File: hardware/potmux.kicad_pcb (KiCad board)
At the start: 2 copper layers, 22.9 x 29.2 mm, 8 parts, among them P1 SOCKET_LEFT, P3 SOCKET_RIGHT, P4 KEYMAN64, U1 4052, U2 4052

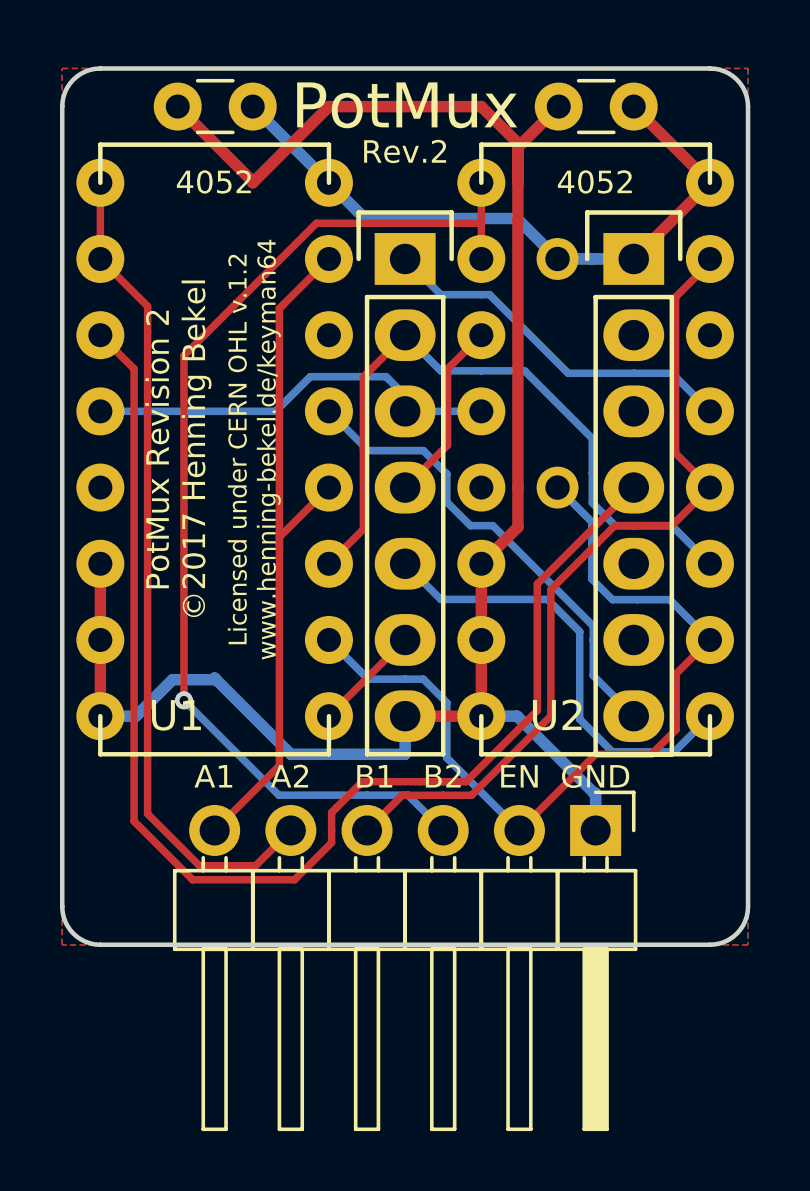
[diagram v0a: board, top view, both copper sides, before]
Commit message: Changes in preparation for release
- Changed Licenses to MIT-style licensing schemes
- Removed files required by cern ohl
- Rerendered schematic svg
- Improved silkscreen, updated last name and Copyright notices
- Adjustments for KiCAD 5.x
- Improved Makefile
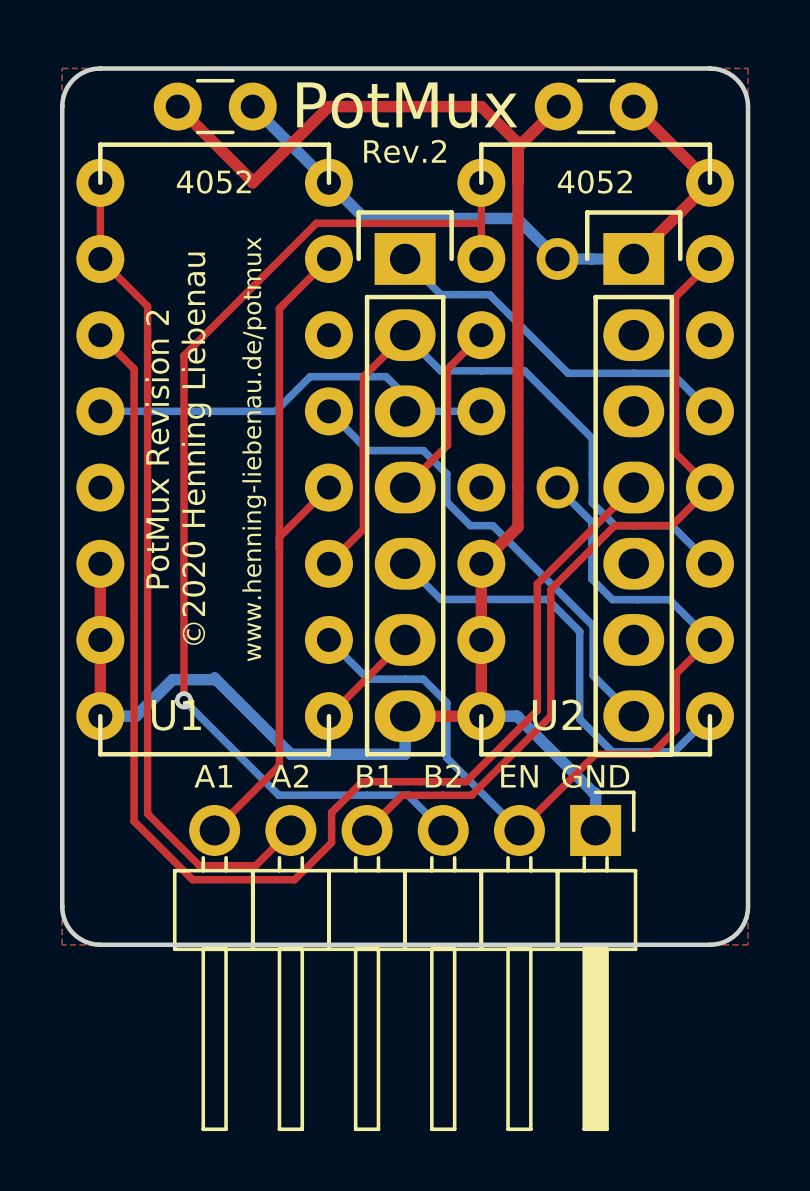
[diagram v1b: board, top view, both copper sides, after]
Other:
- board text added: "PotMux Revision 2 ©2020 Henning Liebenau"
- board text added: "www.henning-liebenau.de/potmux"
- board text removed: "Licensed under CERN OHL v.1.2 www.henning-bekel.de/keyman64"
- board text removed: "PotMux Revision 2 ©2017 Henning Bekel"
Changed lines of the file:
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@@
-(kicad_pcb (version 4) (host pcbnew 4.0.4-stable)
+(kicad_pcb (version 20171130) (host pcbnew 5.1.6)
   (general
-    (links 35)
-    (no_connects 0)
-    (area 126.673238 87.925 174.22 141.130001)
     (thickness 1.6)
     (drawings 22)
@@
     (zone_45_only no)
     (trace_min 0.2)
-    (segment_width 0.2)
-    (edge_width 0.15)
     (via_size 0.6)
     (via_drill 0.4)
@@
     (uvia_min_size 0.2)
     (uvia_min_drill 0.1)
+    (edge_width 0.15)
+    (segment_width 0.2)
     (pcb_text_width 0.3)
     (pcb_text_size 1.5 1.5)
@@
     (visible_elements 7FFFFFFF)
     (pcbplotparams
-      (layerselection 0x010f0_80000001)
+      (layerselection 0x010f0_ffffffff)
       (usegerberextensions true)
       (usegerberattributes true)
+      (usegerberadvancedattributes true)
+      (creategerberjobfile true)
       (excludeedgelayer true)
       (linewidth 0.100000)
@@
       (hpglpennumber 1)
       (hpglpenspeed 20)
-      (hpglpendiameter 15)
-      (hpglpenoverlay 2)
+      (hpglpendiameter 15.000000)
       (psnegative false)
       (psa4output false)
@@
       (drillshape 0)
       (scaleselection 1)
-      (outputdirectory gerber/))
+      (outputdirectory "./gerber"))
   )
   (net 0 "")
@@
     (pad 7 thru_hole oval (at 0 15.24) (size 2.032 1.7272) (drill 1.016) (layers *.Cu *.Mask F.SilkS)
       (net 2 GND))
-    (model Pin_Headers.3dshapes/Pin_Header_Straight_1x07.wrl
-      (at (xyz 0 -0.3 -0.06))
+    (model ${KISYS3DMOD}/Pin_Headers.3dshapes/Pin_Header_Straight_1x07_Pitch2.54mm.wrl
+      (offset (xyz 0 0 -7.5))
       (scale (xyz 1 1 1))
-      (rotate (xyz 0 180 90))
+      (rotate (xyz 0 0 0))
     )
   )
@@
       (net 15 /POTAX))
     (model Pin_Headers.3dshapes/Pin_Header_Straight_1x07.wrl
-      (at (xyz 0 -0.3 -0.06))
+      (offset (xyz 0 -7.619999885559082 -1.523999977111816))
       (scale (xyz 1 1 1))
       (rotate (xyz 0 180 90))
@@
     (descr "Through hole angled pin header, 1x06, 2.54mm pitch, 6mm pin length, single row")
     (tags "Through hole angled pin header THT 1x06 2.54mm single row")
-    (fp_text reference P4 (at 6.604 6.35 360) (layer F.Fab)
-      (effects (font (size 1 1) (thickness 0.15)))
-    )
-    (fp_text value KEYMAN64 (at 8.89 -5.08 360) (layer F.Fab)
+    (fp_text reference P4 (at 6.604 6.35) (layer F.Fab)
+      (effects (font (size 1 1) (thickness 0.15)))
+    )
+    (fp_text value KEYMAN64 (at 8.89 -5.08) (layer F.Fab)
       (effects (font (size 1 1) (thickness 0.15)))
     )
@@
     (fp_line (start 10.4 14.5) (end 10.4 -1.8) (layer F.CrtYd) (width 0.05))
     (fp_line (start 10.4 -1.8) (end -1.8 -1.8) (layer F.CrtYd) (width 0.05))
-    (fp_text user %R (at 7.62 -5.08 360) (layer F.Fab)
+    (fp_text user %R (at 7.62 -5.08) (layer F.Fab)
       (effects (font (size 1 1) (thickness 0.15)))
     )
@@
     (pad 6 thru_hole oval (at 0 12.7 270) (size 1.7 1.7) (drill 1) (layers *.Cu *.Mask)
       (net 9 /A1))
-    (model ${KISYS3DMOD}/Pin_Headers.3dshapes/Pin_Header_Angled_1x06.wrl
-      (at (xyz 0 -0.25 0))
+    (model ${KISYS3DMOD}/Pin_Headers.3dshapes/Pin_Header_Angled_1x06_Pitch2.54mm.wrl
+      (at (xyz 0 0 0))
       (scale (xyz 1 1 1))
-      (rotate (xyz 0 0 90))
+      (rotate (xyz 0 0 0))
     )
   )
@@
     (model Capacitors_THT.3dshapes/C_Disc_D3.0mm_W1.6mm_P2.50mm.wrl
       (at (xyz 0 0 0))
-      (scale (xyz 0.393701 0.393701 0.393701))
+      (scale (xyz 1 1 1))
       (rotate (xyz 0 0 0))
     )
@@
     (model Capacitors_THT.3dshapes/C_Disc_D3.0mm_W1.6mm_P2.50mm.wrl
       (at (xyz 0 0 0))
-      (scale (xyz 0.393701 0.393701 0.393701))
+      (scale (xyz 1 1 1))
       (rotate (xyz 0 0 0))
     )
@@
   (gr_line (start 153.67 118.11) (end 153.67 91.44) (angle 90) (layer Edge.Cuts) (width 0.15))
   (gr_line (start 132.08 119.38) (end 152.4 119.38) (angle 90) (layer Edge.Cuts) (width 0.15))
-  (gr_text "Licensed under CERN OHL v.1.2\nwww.henning-bekel.de/keyman64" (at 137.16 102.87 90) (layer F.SilkS)
+  (gr_text www.henning-liebenau.de/potmux (at 137.16 102.87 90) (layer F.SilkS)
     (effects (font (size 0.6 0.6) (thickness 0.15)))
   )
@@
     (effects (font (size 0.75 0.75) (thickness 0.15)))
   )
-  (gr_text "PotMux Revision 2\n©2017 Henning Bekel" (at 134.62 102.87 90) (layer F.SilkS)
-    (effects (font (size 0.75 0.75) (thickness 0.15)))
-  )
+  (gr_text "PotMux Revision 2\n©2020 Henning Liebenau" (at 134.62 102.87 90) (layer F.SilkS)
+    (effects (font (size 0.75 0.75) (thickness 0.15)))
+  )
